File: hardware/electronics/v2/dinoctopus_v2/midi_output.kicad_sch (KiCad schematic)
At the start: 5 parts, among them J11-O1 SJ-3524-SMT

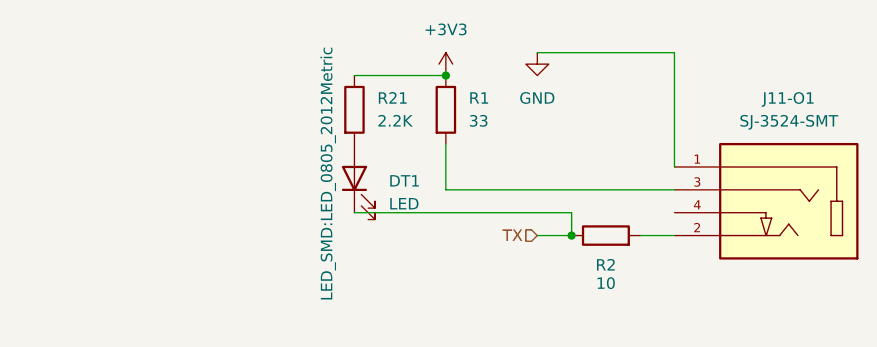
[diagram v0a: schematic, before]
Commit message: Rework schemas with JLCPCB references
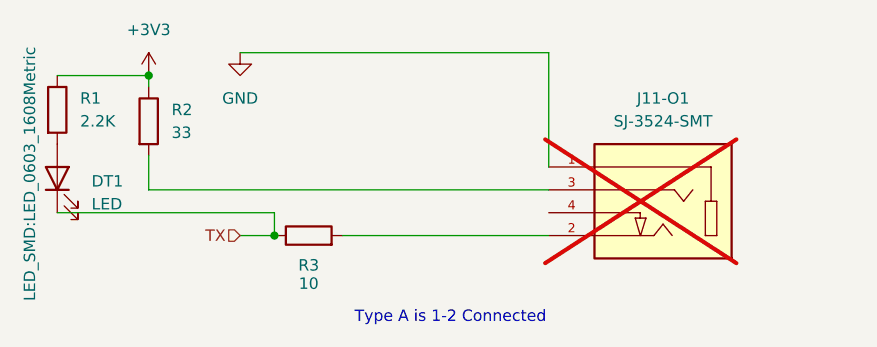
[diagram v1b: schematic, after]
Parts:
- removed R21: 2.2K, Resistor_SMD:R_1206_3216Metric_Pad1.30x1.75mm_HandSolder, symbol Device:R
- added R3: 10, Resistor_SMD:R_0805_2012Metric, symbol Device:R
- DT1: footprint LED_SMD:LED_0805_2012Metric -> LED_SMD:LED_0603_1608Metric; LCSC (none) -> C72038
- J11-O1: footprint MIDI_projects:CUI_SJ-3524-SMT -> Library:CUI_SJ-3524-SMT; now not fitted; now left out of the parts list
- R1: value 33 -> 2.2K; footprint Resistor_SMD:R_1206_3216Metric_Pad1.30x1.75mm_HandSolder -> Resistor_SMD:R_0805_2012Metric; LCSC (none) -> C17520
- R2: value 10 -> 33; footprint Resistor_SMD:R_1206_3216Metric_Pad1.30x1.75mm_HandSolder -> Resistor_SMD:R_0805_2012Metric; LCSC (none) -> C17634
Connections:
- net +3V3: now also R2.1
- net TX: now also R3.1; no longer R2.1
- net at DT1.2 (A): now also R1.2
- net at J11-O1.3: now also R2.2; no longer R1.2
- net at J11-O1.2: now also R3.2; no longer R2.2
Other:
- note added: "Type A is 1-2 Connected"
